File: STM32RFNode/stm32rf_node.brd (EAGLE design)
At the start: 100 x 80 mm, 6 parts

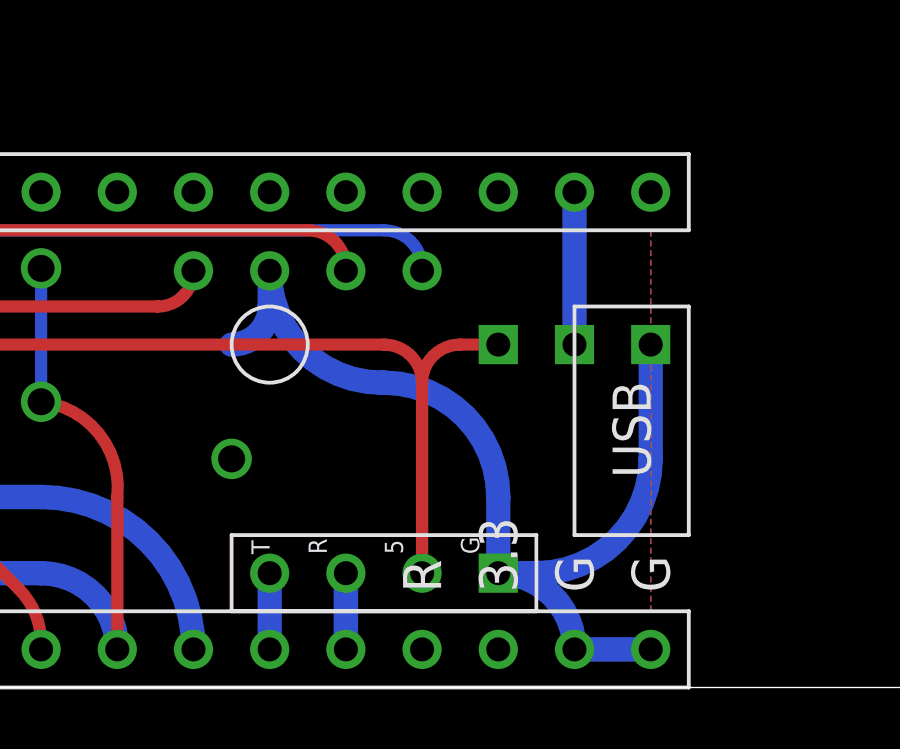
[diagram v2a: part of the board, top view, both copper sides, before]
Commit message: Added possibility to connect the MPU 6050 on the I2C by shifting connections to match Add with Gnd
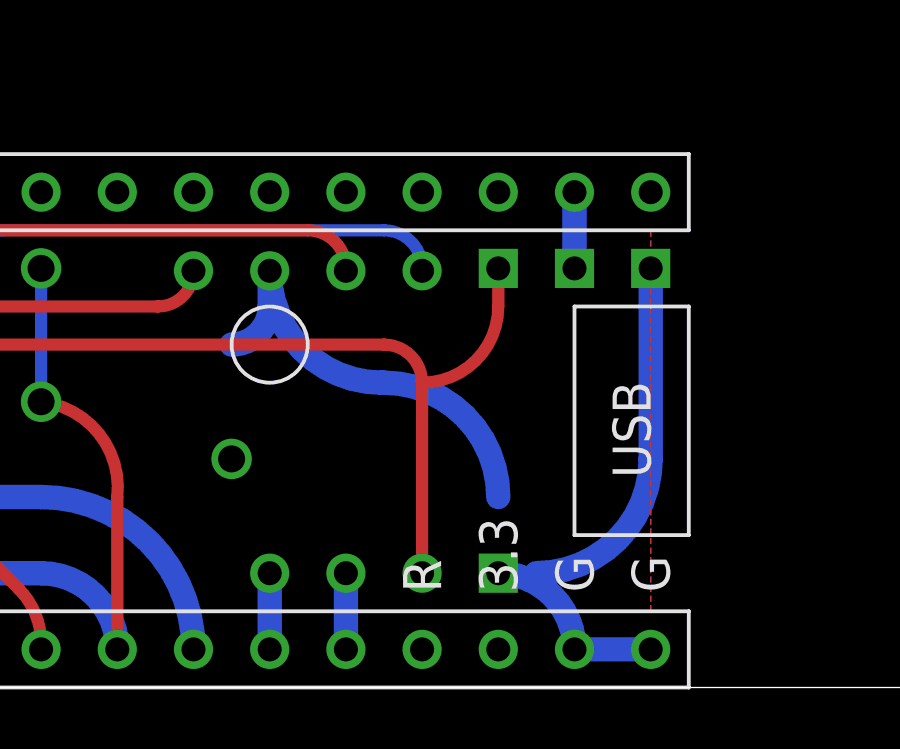
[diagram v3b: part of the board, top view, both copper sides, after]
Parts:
- U$5: value ONE_WIRE -> ONE_WIRE'RIGHT'; device one-wire:ONE_WIRE -> one-wire:ONE_WIRE_RIGHT
- moved U$5 2.54 mm to (47.0, 14.0)
- flipped U$6 to the bottom, turned to 270 degrees
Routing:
- net N$12: track 5.08 -> 2.54 mm
- net 5V: track 48.4 -> 50.1 mm
- net GND: track 56.3 -> 55.0 mm
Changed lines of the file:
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@@
 </class>
 </classes>
-<designrules name="default">
+<designrules name="EagleRules">
 <description language="de">&lt;b&gt;EAGLE Design Rules&lt;/b&gt;
 &lt;p&gt;
@@
 necessary adjustments and save your customized
 design rules under a new name.</description>
+<description language="zh">&lt;b&gt;NOA-Labs EAGLE Design Rules&lt;/b&gt;
+</description>
 <param name="layerSetup" value="(1*16)"/>
 <param name="mtCopper" value="0.035mm 0.035mm 0.035mm 0.035mm 0.035mm 0.035mm 0.035mm 0.035mm 0.035mm 0.035mm 0.035mm 0.035mm 0.035mm 0.035mm 0.035mm 0.035mm"/>
 <param name="mtIsolate" value="1.5mm 0.15mm 0.2mm 0.15mm 0.2mm 0.15mm 0.2mm 0.15mm 0.2mm 0.15mm 0.2mm 0.15mm 0.2mm 0.15mm 0.2mm"/>
-<param name="mdWireWire" value="8mil"/>
-<param name="mdWirePad" value="8mil"/>
-<param name="mdWireVia" value="8mil"/>
-<param name="mdPadPad" value="8mil"/>
-<param name="mdPadVia" value="8mil"/>
-<param name="mdViaVia" value="8mil"/>
-<param name="mdSmdPad" value="8mil"/>
-<param name="mdSmdVia" value="8mil"/>
-<param name="mdSmdSmd" value="8mil"/>
+<param name="mdWireWire" value="7mil"/>
+<param name="mdWirePad" value="7mil"/>
+<param name="mdWireVia" value="7mil"/>
+<param name="mdPadPad" value="7mil"/>
+<param name="mdPadVia" value="7mil"/>
+<param name="mdViaVia" value="7mil"/>
+<param name="mdSmdPad" value="0mil"/>
+<param name="mdSmdVia" value="0mil"/>
+<param name="mdSmdSmd" value="0mil"/>
 <param name="mdViaViaSameLayer" value="8mil"/>
 <param name="mnLayersViaInSmd" value="2"/>
-<param name="mdCopperDimension" value="40mil"/>
-<param name="mdDrill" value="8mil"/>
+<param name="mdCopperDimension" value="20mil"/>
+<param name="mdDrill" value="10mil"/>
 <param name="mdSmdStop" value="0mil"/>
-<param name="msWidth" value="10mil"/>
-<param name="msDrill" value="24mil"/>
-<param name="msMicroVia" value="9.99mm"/>
+<param name="msWidth" value="7mil"/>
+<param name="msDrill" value="12mil"/>
+<param name="msMicroVia" value="12mil"/>
 <param name="msBlindViaRatio" value="0.5"/>
 <param name="rvPadTop" value="0.25"/>
@@
 <param name="rlMinPadBottom" value="10mil"/>
 <param name="rlMaxPadBottom" value="20mil"/>
-<param name="rlMinViaOuter" value="8mil"/>
+<param name="rlMinViaOuter" value="6mil"/>
 <param name="rlMaxViaOuter" value="20mil"/>
-<param name="rlMinViaInner" value="8mil"/>
+<param name="rlMinViaInner" value="6mil"/>
 <param name="rlMaxViaInner" value="20mil"/>
 <param name="rlMinMicroViaOuter" value="4mil"/>
@@
 <param name="psTop" value="-1"/>
 <param name="psBottom" value="-1"/>
-<param name="psFirst" value="-1"/>
+<param name="psFirst" value="0"/>
 <param name="psElongationLong" value="100"/>
 <param name="psElongationOffset" value="100"/>
 <param name="mvStopFrame" value="1"/>
 <param name="mvCreamFrame" value="0"/>
-<param name="mlMinStopFrame" value="4mil"/>
-<param name="mlMaxStopFrame" value="4mil"/>
+<param name="mlMinStopFrame" value="2mil"/>
+<param name="mlMaxStopFrame" value="2mil"/>
 <param name="mlMinCreamFrame" value="0mil"/>
 <param name="mlMaxCreamFrame" value="0mil"/>
-<param name="mlViaStopLimit" value="0mil"/>
+<param name="mlViaStopLimit" value="25mil"/>
 <param name="srRoundness" value="0"/>
 <param name="srMinRoundness" value="0mil"/>
@@
 <param name="checkAngle" value="0"/>
 <param name="checkFont" value="1"/>
-<param name="checkRestrict" value="1"/>
+<param name="checkRestrict" value="0"/>
 <param name="useDiameter" value="13"/>
 <param name="maxErrors" value="50"/>
@@
 <element name="U$3" library="GY-BMEP" package="GY-BMEP-NOHOLE" value="GY-BMEPGY-BMEP-NOHOLE" x="38.1" y="8.89" rot="MR270"/>
 <element name="U$4" library="GY-49" package="GY-49-SURF" value="GY-49G-49-SURF" x="22.86" y="8.89" rot="MR270"/>
-<element name="U$5" library="one-wire" package="ONE_WIRE" value="ONE_WIRE" x="46.99" y="11.43" rot="MR270"/>
-<element name="U$6" library="WFConnectors" package="UART-MINI" value="UARTMINI" x="44.45" y="3.81" rot="R90"/>
+<element name="U$5" library="one-wire" package="ONE_WIRE_RIGHT" value="ONE_WIRE'RIGHT'" x="46.99" y="13.97" rot="MR270"/>
+<element name="U$6" library="WFConnectors" package="UART-MINI" value="UARTMINI" x="44.45" y="3.81" rot="MR270"/>
 </elements>
 <signals>
@@
 <contactref element="U$1" pad="GND@3"/>
 <wire x1="49.53" y1="1.27" x2="46.99" y2="1.27" width="0.8128" layer="16"/>
-<wire x1="46.99" y1="1.27" x2="44.45" y2="3.81" width="0.8128" layer="16" curve="90"/>
-<wire x1="44.45" y1="3.81" x2="45.72" y2="3.81" width="0.8128" layer="16"/>
 <wire x1="45.72" y1="3.81" x2="49.53" y2="7.62" width="0.8128" layer="16" curve="90"/>
-<wire x1="49.53" y1="7.62" x2="49.53" y2="11.43" width="0.8128" layer="16"/>
-<wire x1="44.45" y1="3.81" x2="44.45" y2="6.35" width="0.8128" layer="16"/>
+<wire x1="49.53" y1="7.62" x2="49.53" y2="13.97" width="0.8128" layer="16"/>
 <wire x1="44.45" y1="6.35" x2="40.64" y2="10.16" width="0.8128" layer="16" curve="90"/>
 <wire x1="40.64" y1="10.16" x2="40.56" y2="10.16" width="0.8128" layer="16"/>
@@
 <via x="35.56" y="7.62" extent="1-16" drill="0.9"/>
 <via x="25.4" y="8.89" extent="1-16" drill="0.9"/>
+<wire x1="46.99" y1="1.27" x2="44.45" y2="3.81" width="0.8128" layer="16" curve="90"/>
 </signal>
 <signal name="3V3">
@@
 <contactref element="U$6" pad="2"/>
 <contactref element="U$1" pad="5V"/>
-<wire x1="44.45" y1="11.43" x2="43.18" y2="11.43" width="0.4064" layer="1"/>
-<wire x1="43.18" y1="11.43" x2="41.91" y2="10.16" width="0.4064" layer="1" curve="90"/>
-<wire x1="41.91" y1="10.16" x2="41.91" y2="3.81" width="0.4064" layer="1"/>
-<wire x1="41.91" y1="10.16" x2="40.64" y2="11.43" width="0.4064" layer="1" curve="90"/>
+<wire x1="40.64" y1="11.43" x2="41.91" y2="10.16" width="0.4064" layer="1" curve="-90"/>
 <wire x1="18.415" y1="11.43" x2="17.78" y2="12.065" width="0.4064" layer="1" curve="-90"/>
 <wire x1="17.78" y1="12.065" x2="17.145" y2="12.7" width="0.4064" layer="1" curve="90"/>
@@
 <wire x1="40.64" y1="11.43" x2="18.415" y2="11.43" width="0.4064" layer="1"/>
 <wire x1="17.145" y1="12.7" x2="8.89" y2="12.7" width="0.4064" layer="1"/>
+<wire x1="41.91" y1="3.81" x2="41.91" y2="10.16" width="0.4064" layer="1"/>
+<wire x1="41.91" y1="10.16" x2="44.45" y2="12.7" width="0.4064" layer="1" curve="90"/>
+<wire x1="44.45" y1="12.7" x2="44.45" y2="13.97" width="0.4064" layer="1"/>
 </signal>
 <signal name="N$7">
 <contactref element="U$6" pad="4"/>
 <contactref element="U$1" pad="PB_10"/>
-<wire x1="36.83" y1="1.27" x2="36.83" y2="3.81" width="0.8128" layer="16"/>
+<wire x1="36.83" y1="3.81" x2="36.83" y2="1.27" width="0.8128" layer="16"/>
 </signal>
 <signal name="N$8">
 <contactref element="U$1" pad="PB_11"/>
 <contactref element="U$6" pad="3"/>
-<wire x1="39.37" y1="1.27" x2="39.37" y2="3.81" width="0.8128" layer="16"/>
+<wire x1="39.37" y1="3.81" x2="39.37" y2="1.27" width="0.8128" layer="16"/>
 </signal>
 <signal name="N$9">
@@
 <contactref element="U$1" pad="PB_13"/>
 <contactref element="U$5" pad="S"/>
-<wire x1="46.99" y1="16.51" x2="46.99" y2="11.43" width="0.8128" layer="16"/>
+<wire x1="46.99" y1="16.51" x2="46.99" y2="13.97" width="0.8128" layer="16"/>
 </signal>
 </signals>

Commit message: preparing production 1
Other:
- board size 100 x 80 mm -> 50.8 x 17.8 mm
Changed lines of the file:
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@@
 <setting verticaltext="up"/>
 </settings>
-<grid distance="0.05" unitdist="inch" unit="inch" style="lines" multiple="1" display="yes" altdistance="0.025" altunitdist="inch" altunit="inch"/>
+<grid distance="0.05" unitdist="inch" unit="mm" style="lines" multiple="1" display="yes" altdistance="0.025" altunitdist="inch" altunit="inch"/>
 <layers>
 <layer number="1" name="Top" color="4" fill="1" visible="yes" active="yes"/>
@@
 <board>
 <plain>
-<wire x1="0" y1="0" x2="100" y2="0" width="0" layer="20"/>
-<wire x1="100" y1="0" x2="100" y2="80" width="0" layer="20"/>
-<wire x1="100" y1="80" x2="0" y2="80" width="0" layer="20"/>
-<wire x1="0" y1="80" x2="0" y2="0" width="0" layer="20"/>
+<wire x1="0" y1="0" x2="50.8" y2="0" width="0" layer="20"/>
+<wire x1="50.8" y1="0" x2="50.8" y2="17.77" width="0" layer="20"/>
+<wire x1="50.8" y1="17.77" x2="0" y2="17.77" width="0" layer="20"/>
+<wire x1="0" y1="17.77" x2="0" y2="0" width="0" layer="20"/>
 </plain>
 <attributes>
